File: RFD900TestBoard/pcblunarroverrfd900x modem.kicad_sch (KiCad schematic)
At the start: 26 parts, among them J1 Barrel_Jack, J10 Conn_02x01, J11 Conn_02x01, J12 Conn_02x01, J13 Conn_02x01, J14 Conn_02x01, J16 Conn_02x01, J17 Conn_02x01, J18 Conn_01x11, J2 Conn_02x08_Counter_Clockwise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

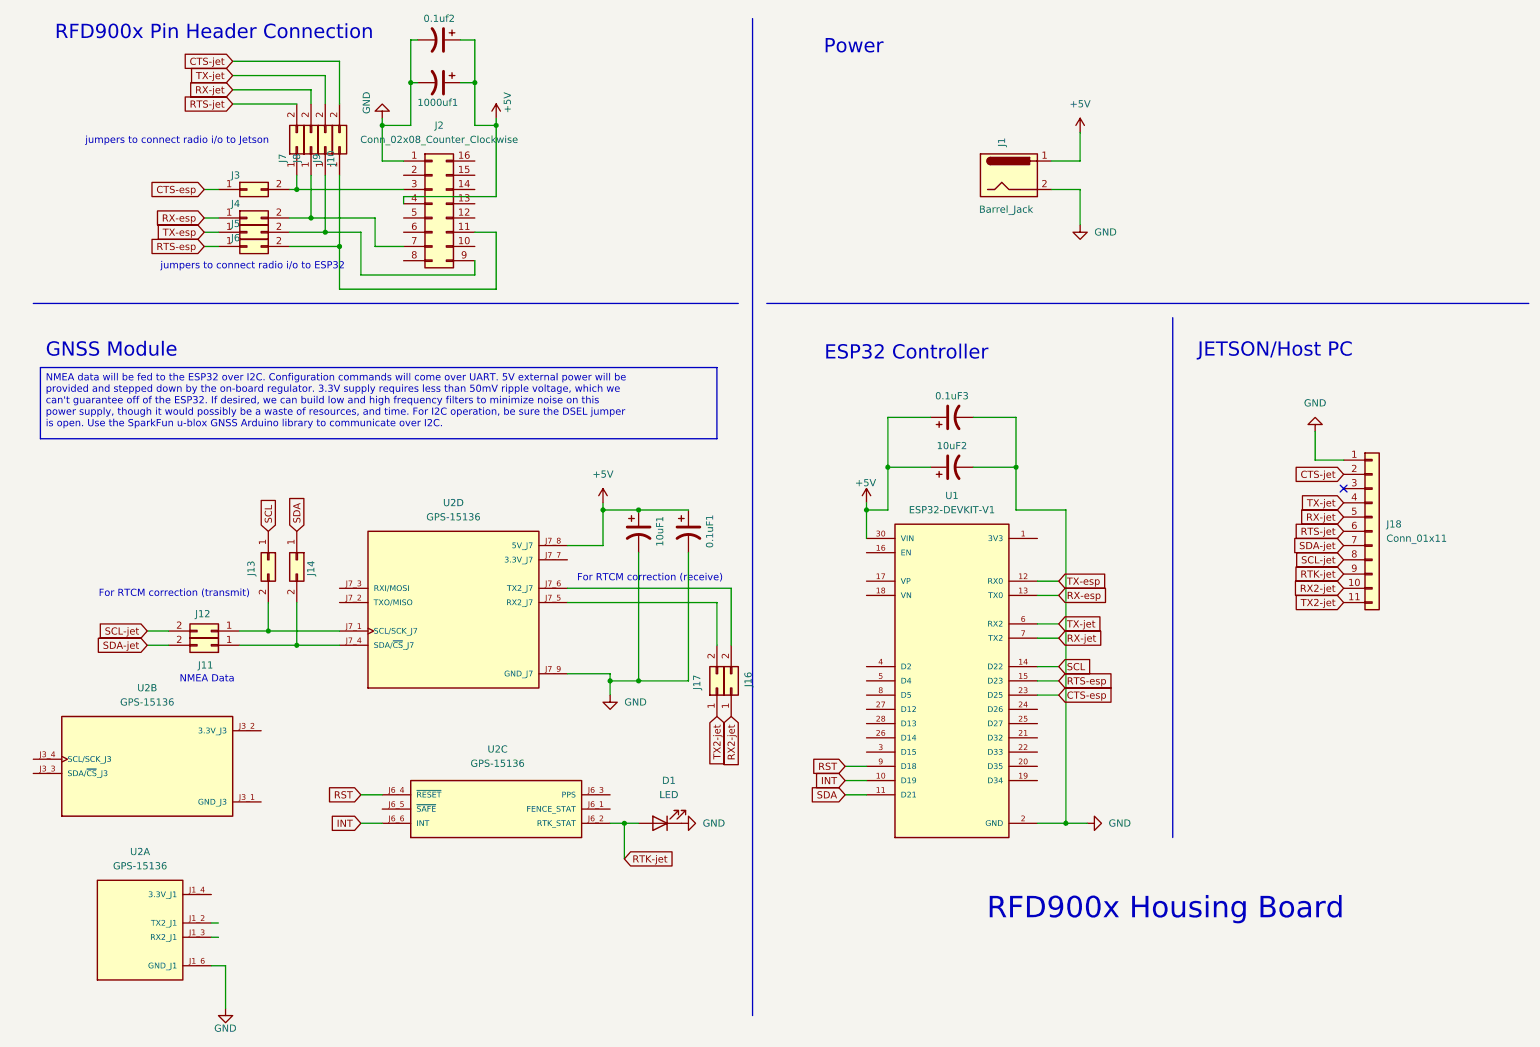
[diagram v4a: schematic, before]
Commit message: made some changes to the layout of the RFD900x housing board
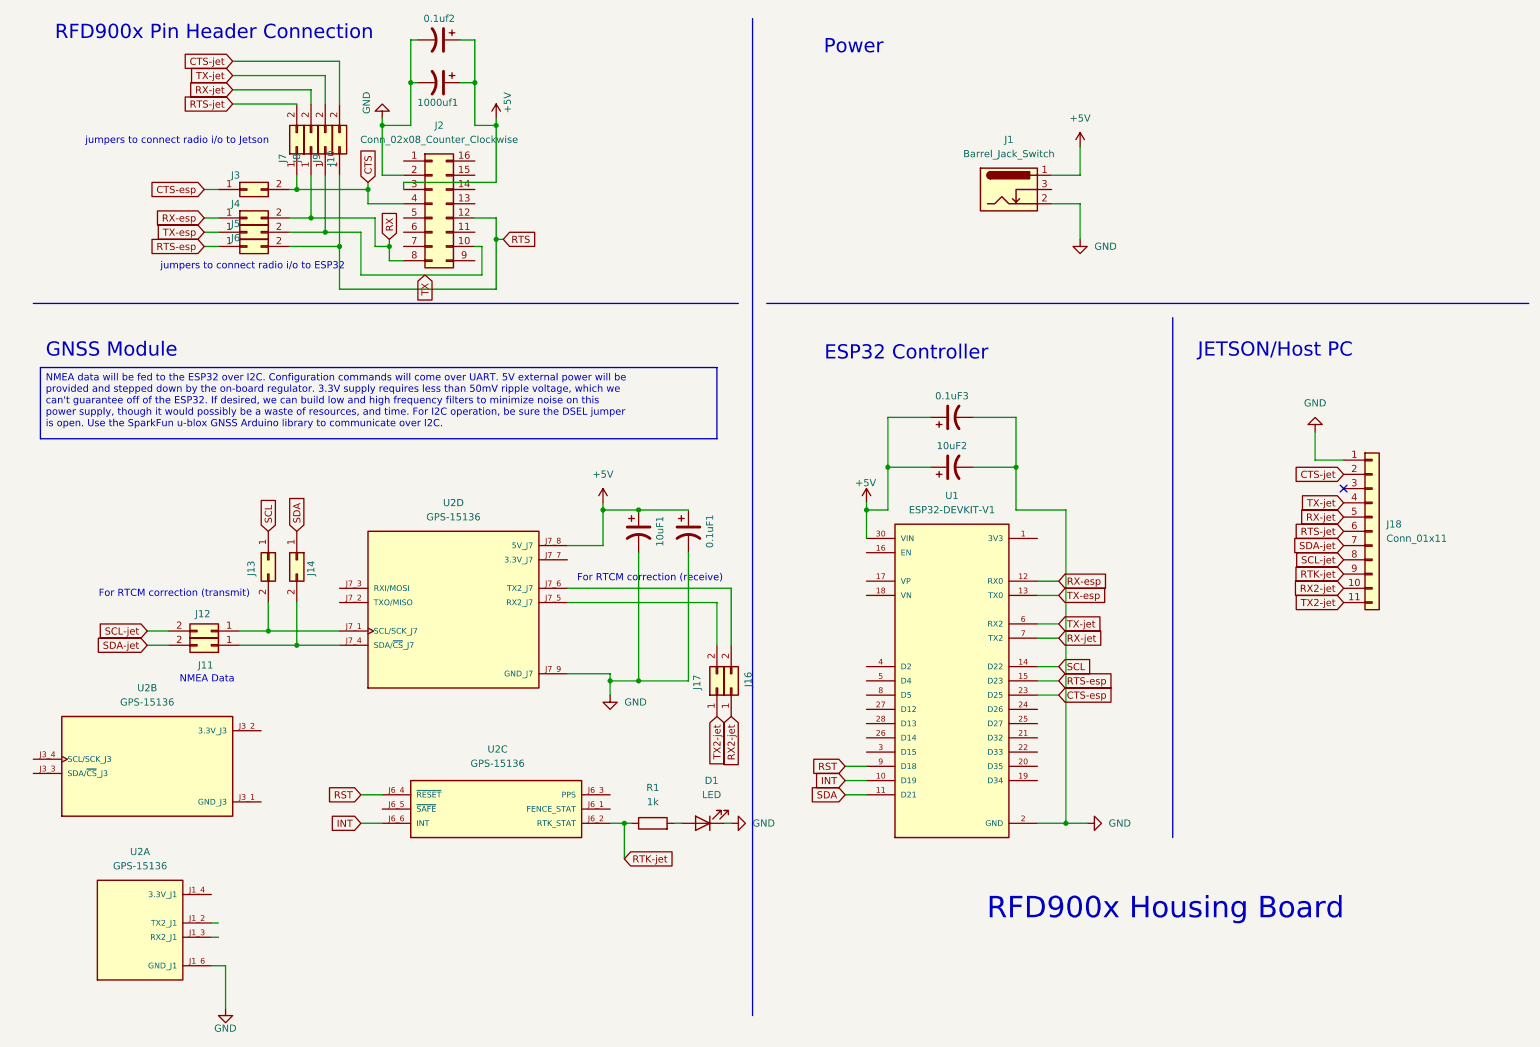
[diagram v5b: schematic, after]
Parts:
- removed J1: Barrel_Jack, Connector_BarrelJack:BarrelJack_SwitchcraftConxall_RAPC10U_Horizontal, symbol Connector:Barrel_Jack
- added J1: Barrel_Jack_Switch, Connector_BarrelJack:BarrelJack_Horizontal, symbol Connector:Barrel_Jack_Switch
- added R1: 1k, Resistor_THT:R_Axial_DIN0204_L3.6mm_D1.6mm_P2.54mm_Vertical, symbol Device:R
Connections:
- net +5V: now also J2.3 (Pin_3), J1.1; no longer J2.4 (Pin_4)
- net GND: now also J2.2 (Pin_2), J1.2; no longer J2.1 (Pin_1)
- net RTK-jet: now also R1.1; no longer D1.2 (A)
- net RX-esp: now also U1.12 (RX0); no longer U1.13 (TX0)
- net TX-esp: now also U1.13 (TX0); no longer U1.12 (RX0)
- net TX: now reaches J5.2 (Pin_2), J9.1 (Pin_1)
- net TX: now also J2.10 (Pin_10); no longer J2.9 (Pin_9)
- net CTS: now reaches J3.2 (Pin_2), J7.1 (Pin_1)
- net CTS: now also J2.4 (Pin_4); no longer J2.3 (Pin_3)
- net RX: now reaches J4.2 (Pin_2), J8.1 (Pin_1)
- net RX: now also J2.8 (Pin_8); no longer J2.7 (Pin_7)
- net RTS: now reaches J10.1 (Pin_1), J6.2 (Pin_2)
- net RTS: now also J2.12 (Pin_12); no longer J2.11 (Pin_11)
- new net: D1.2 (A), R1.2
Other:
- moved on the sheet: D1

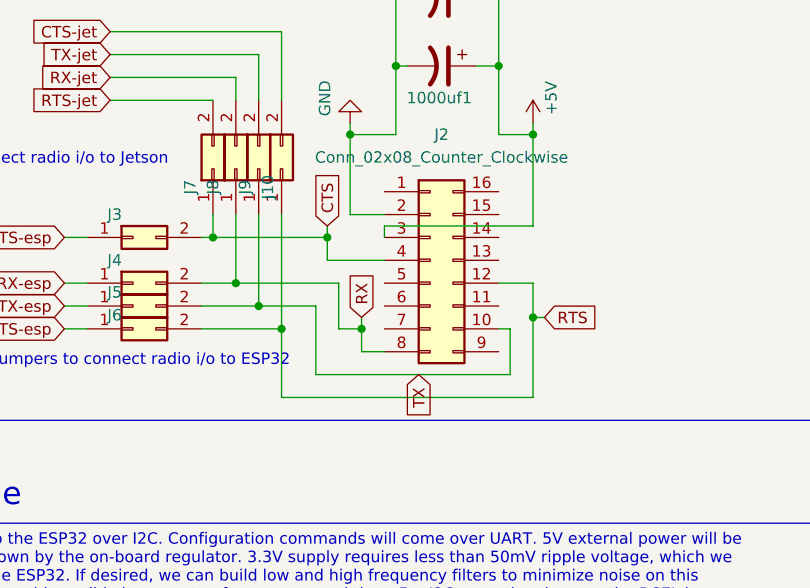
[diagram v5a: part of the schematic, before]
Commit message: made final changes to RFD900x Housing Board
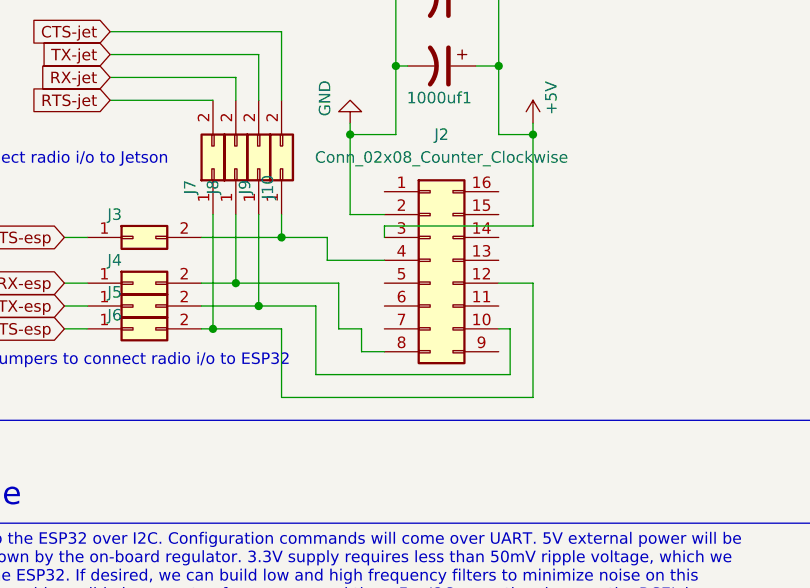
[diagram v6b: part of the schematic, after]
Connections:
- net CTS: no longer names the net of J2.4 (Pin_4), J3.2 (Pin_2)
- net CTS: now also J10.1 (Pin_1); no longer J7.1 (Pin_1)
- net RTS: no longer names the net of J2.12 (Pin_12), J6.2 (Pin_2)
- net RTS: now also J7.1 (Pin_1); no longer J10.1 (Pin_1)
- net RX: no longer names the net of J2.8 (Pin_8), J4.2 (Pin_2), J8.1 (Pin_1)
- net TX: no longer names the net of J2.10 (Pin_10), J5.2 (Pin_2), J9.1 (Pin_1)
